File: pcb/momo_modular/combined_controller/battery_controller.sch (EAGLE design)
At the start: 38 parts, among them Q2 P-MOSFET, U1 XRP7659, U3 MCP1702, U4 PIC24F16KA101-X_PSSOP, U5 FLASH8MSOP8, U6 MCP73811

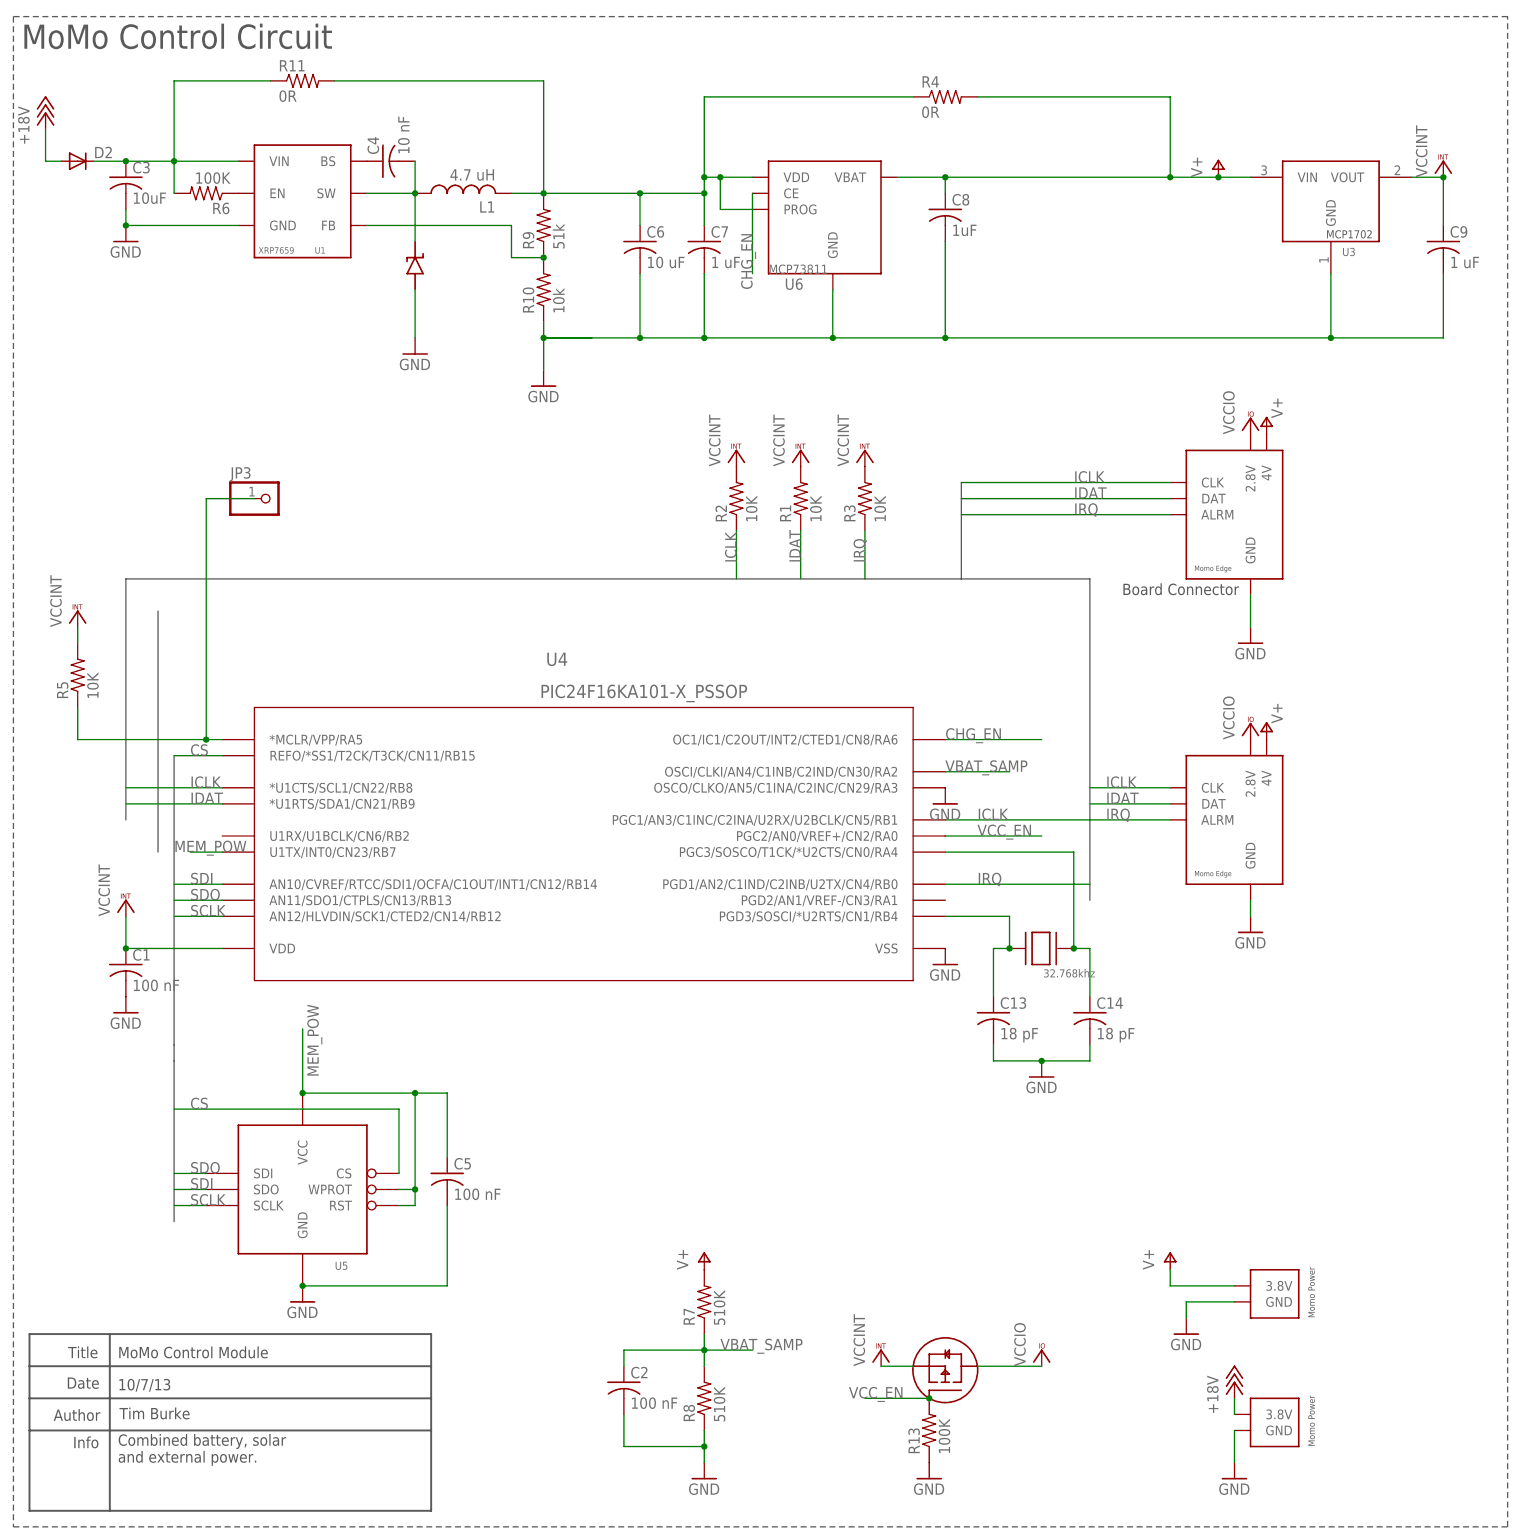
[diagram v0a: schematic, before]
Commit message: Finish initial layout of revised controller board with enhanced pic
- now has battery backup of RTC
- new pic24 chip with 64K rom and 8K RAM
- lower power consumption
- removed current meter to battery for charging current (just measure
  the voltage over time)
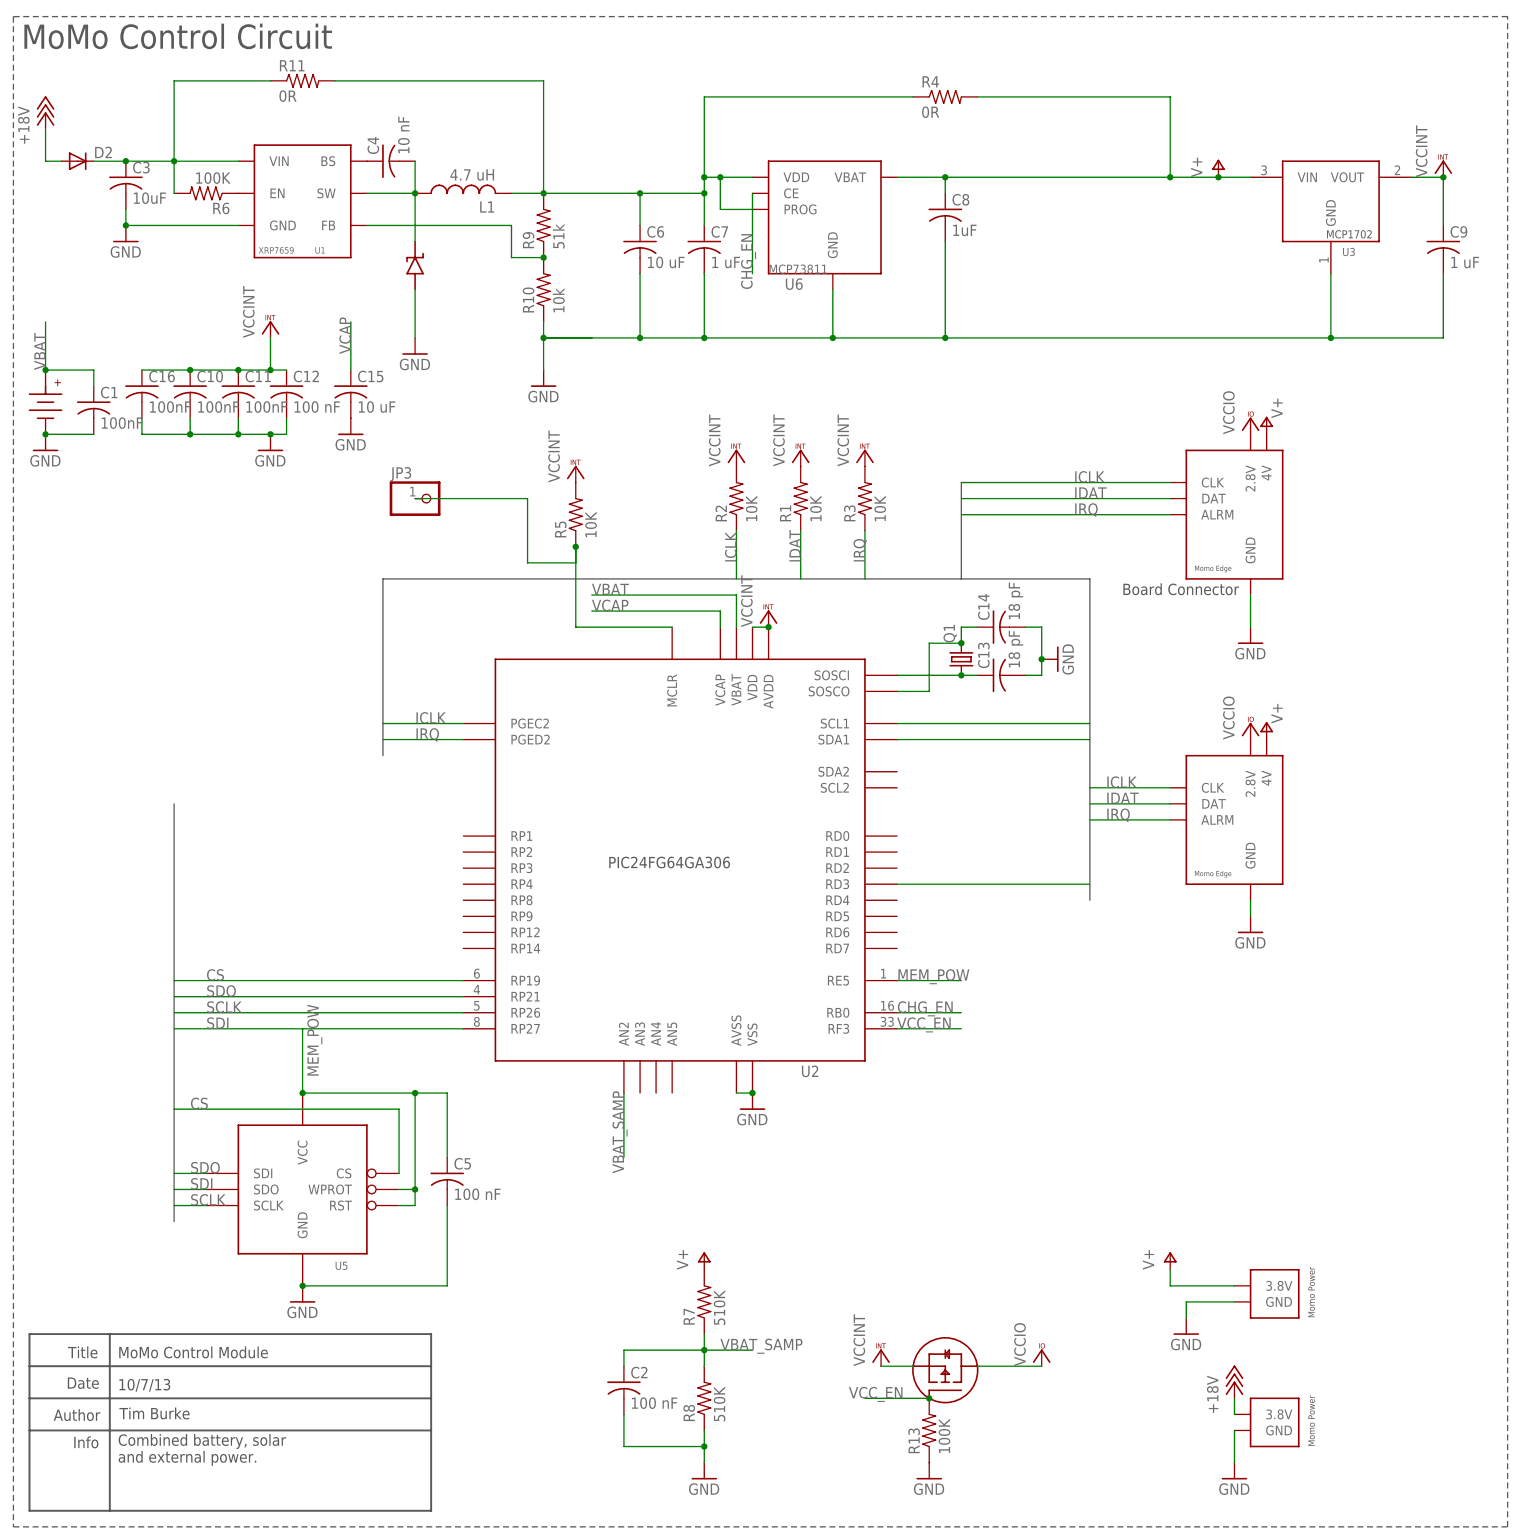
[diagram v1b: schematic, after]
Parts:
- removed U4: PIC24F16KA101-X_PSSOP, components:PIC24F16KA101-X_PSSOP
- removed XT1: 32.768khz, components:SMD-XTAL
- added BATT1: CR1025-HOLDER, components:CR1025-HOLDER
- added C10, C11, C16: 100nF, rcl:C-USC0402
- added C12: 100 nF, rcl:C-USC0402
- added C15: 10 uF, rcl:C-USC0805
- added Q1: (no value), crystal:CRYSTALTC26H
- added U2: PIC24FJ64GA306, components:PIC24FJ64GA306
- C1: value 100 nF -> 100nF; DIGIKEY-PN 445-1265-1-ND -> (none)
- R5: DIGIKEY-PN P10.0KHCT-ND -> (none)
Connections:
- removed net N$15: JP3.1, R5.1, U4.*MCLR/VPP/RA5
- removed net N$24: C14.1, U4.PGC3/SOSCO/T1CK/*U2CTS/CN0/RA4, XT1.XTAL2
- removed net N$25: C13.1, U4.PGD3/SOSCI/*U2RTS/CN1/RB4, XT1.XTAL1
- new net N$4: JP3.1, R5.1, U2.MCLR
- new net N$6: C14.1, Q1.2, U2.SOSCO
- new net N$7: C13.1, Q1.1, U2.SOSCI
- new net VBAT: BATT1.+, C1.1, U2.VBAT
- new net VCAP: C15.1, U2.VCAP
- net CHG_EN: now also U2.RB0; no longer U4.OC1/IC1/C2OUT/INT2/CTED1/CN8/RA6
- net CS: now also U2.RP19; no longer U4.REFO/*SS1/T2CK/T3CK/CN11/RB15
- net GND: now also BATT1.-, C10.2, C11.2, C12.2, C15.2, C16.2, U2.AVSS, U2.VSS; no longer U4.OSCO/CLKO/AN5/C1INA/C2INC/CN29/RA3, U4.VSS
- net ICLK: now also U2.PGEC2, U2.SCL1; no longer U4.*U1CTS/SCL1/CN22/RB8, U4.PGC1/AN3/C1INC/C2INA/U2RX/U2BCLK/CN5/RB1
- net IDAT: now also U2.SDA1; no longer U4.*U1RTS/SDA1/CN21/RB9
- net IRQ: now also U2.PGED2, U2.RD3; no longer U4.PGD1/AN2/C1IND/C2INB/U2TX/CN4/RB0
- net MEM_POW: now also U2.RE5; no longer U4.U1TX/INT0/CN23/RB7
- net SCLK: now also U2.RP26; no longer U4.AN12/HLVDIN/SCK1/CTED2/CN14/RB12
- net SDI: now also U2.RP27; no longer U4.AN10/CVREF/RTCC/SDI1/OCFA/C1OUT/INT1/CN12/RB14
- net SDO: now also U2.RP21; no longer U4.AN11/SDO1/CTPLS/CN13/RB13
- net VBAT_SAMP: now also U2.AN2; no longer U4.OSCI/CLKI/AN4/C1INB/C2IND/CN30/RA2
- net VCCINT: now also C10.1, C11.1, C12.1, C16.1, U2.AVDD, U2.VDD; no longer C1.1, U4.VDD
- net VCC_EN: now also U2.RF3; no longer U4.PGC2/AN0/VREF+/CN2/RA0
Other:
- moved on the sheet: C1, C13, C14, JP3, R5

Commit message: Finish laying out combined_controller board
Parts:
- C1, C10, C11, C12, C16: DIGIKEY-PN (none) -> 445-1265-1-ND
- D2: DESCRIPTION (none) -> Schottky Diode
- Q1: DIGIKEY-PN (none) -> 535-9034-ND
- R5: DIGIKEY-PN (none) -> P10.0KHCT-ND
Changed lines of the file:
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@@
 <?xml version="1.0" encoding="utf-8"?>
 <!DOCTYPE eagle SYSTEM "eagle.dtd">
-<eagle version="6.5.0">
+<eagle version="6.4">
 <drawing>
 <settings>
@@
 <part name="JP3" library="pinhead" deviceset="PINHD-1X1" device=""/>
 <part name="D2" library="diode" deviceset="DIODE-" device="DO214AC">
+<attribute name="DESCRIPTION" value="Schottky Diode "/>
 <attribute name="DIGIKEY-PN" value="SL13HE3/61TGICT-ND"/>
 </part>
@@
 <attribute name="DIGIKEY-PN-SOLAR" value="MCP73811T-420I/OTCT-ND"/>
 </part>
-<part name="Q1" library="crystal" deviceset="CRYSTAL" device="TC26H"/>
-<part name="R5" library="rcl" deviceset="R-US_" device="R0603" value="10K"/>
+<part name="Q1" library="crystal" deviceset="CRYSTAL" device="TC26H">
+<attribute name="DIGIKEY-PN" value="535-9034-ND"/>
+</part>
+<part name="R5" library="rcl" deviceset="R-US_" device="R0603" value="10K">
+<attribute name="DIGIKEY-PN" value="P10.0KHCT-ND"/>
+</part>
 <part name="VCC5" library="supply1" deviceset="VCCINT" device=""/>
 <part name="VCC6" library="supply1" deviceset="VCCINT" device=""/>
@@
 <part name="GND3" library="supply1" deviceset="GND" device=""/>
 <part name="U2" library="components" deviceset="PIC24FJ64GA306" device=""/>
-<part name="C1" library="rcl" deviceset="C-US" device="C0402" value="100nF"/>
-<part name="C10" library="rcl" deviceset="C-US" device="C0402" value="100nF"/>
-<part name="C11" library="rcl" deviceset="C-US" device="C0402" value="100nF"/>
-<part name="C12" library="rcl" deviceset="C-US" device="C0402" value="100 nF"/>
+<part name="C1" library="rcl" deviceset="C-US" device="C0402" value="100nF">
+<attribute name="DIGIKEY-PN" value="445-1265-1-ND"/>
+</part>
+<part name="C10" library="rcl" deviceset="C-US" device="C0402" value="100nF">
+<attribute name="DIGIKEY-PN" value="445-1265-1-ND"/>
+</part>
+<part name="C11" library="rcl" deviceset="C-US" device="C0402" value="100nF">
+<attribute name="DIGIKEY-PN" value="445-1265-1-ND"/>
+</part>
+<part name="C12" library="rcl" deviceset="C-US" device="C0402" value="100 nF">
+<attribute name="DIGIKEY-PN" value="445-1265-1-ND"/>
+</part>
 <part name="VCC7" library="supply1" deviceset="VCCINT" device=""/>
 <part name="GND5" library="supply1" deviceset="GND" device=""/>
@@
 </part>
 <part name="GND6" library="supply1" deviceset="GND" device=""/>
-<part name="C16" library="rcl" deviceset="C-US" device="C0402" value="100nF"/>
+<part name="C16" library="rcl" deviceset="C-US" device="C0402" value="100nF">
+<attribute name="DIGIKEY-PN" value="445-1265-1-ND"/>
+</part>
 </parts>
 <sheets>
@@
 <instance part="D2" gate="G$1" x="-215.9" y="104.14">
 <attribute name="DIGIKEY-PN" x="-215.9" y="104.14" size="1.778" layer="96" display="off"/>
+<attribute name="DESCRIPTION" x="-215.9" y="104.14" size="1.778" layer="96" display="off"/>
 </instance>
 <instance part="U6" gate="G$1" x="-106.68" y="93.98" smashed="yes">
@@
 <attribute name="DIGIKEY-PN-SOLAR" x="-106.68" y="93.98" size="1.778" layer="96" display="off"/>
 </instance>
-<instance part="Q1" gate="G$1" x="-76.2" y="25.4" rot="R90"/>
-<instance part="R5" gate="G$1" x="-137.16" y="48.26" rot="R90"/>
+<instance part="Q1" gate="G$1" x="-76.2" y="25.4" rot="R90">
+<attribute name="DIGIKEY-PN" x="-76.2" y="25.4" size="1.778" layer="96" rot="R90" display="off"/>
+</instance>
+<instance part="R5" gate="G$1" x="-137.16" y="48.26" rot="R90">
+<attribute name="DIGIKEY-PN" x="-137.16" y="48.26" size="1.778" layer="96" rot="R90" display="off"/>
+</instance>
 <instance part="VCC5" gate="G$1" x="-137.16" y="55.88"/>
 <instance part="VCC6" gate="G$1" x="-106.68" y="33.02"/>
@@
 <instance part="GND3" gate="1" x="-220.98" y="58.42"/>
 <instance part="U2" gate="G$1" x="-104.14" y="-7.62"/>
-<instance part="C1" gate="G$1" x="-213.36" y="66.04"/>
-<instance part="C10" gate="G$1" x="-198.12" y="68.58"/>
-<instance part="C11" gate="G$1" x="-190.5" y="68.58"/>
-<instance part="C12" gate="G$1" x="-182.88" y="68.58"/>
+<instance part="C1" gate="G$1" x="-213.36" y="66.04">
+<attribute name="DIGIKEY-PN" x="-213.36" y="66.04" size="1.778" layer="96" display="off"/>
+</instance>
+<instance part="C10" gate="G$1" x="-198.12" y="68.58">
+<attribute name="DIGIKEY-PN" x="-198.12" y="68.58" size="1.778" layer="96" display="off"/>
+</instance>
+<instance part="C11" gate="G$1" x="-190.5" y="68.58">
+<attribute name="DIGIKEY-PN" x="-190.5" y="68.58" size="1.778" layer="96" display="off"/>
+</instance>
+<instance part="C12" gate="G$1" x="-182.88" y="68.58">
+<attribute name="DIGIKEY-PN" x="-182.88" y="68.58" size="1.778" layer="96" display="off"/>
+</instance>
 <instance part="VCC7" gate="G$1" x="-185.42" y="78.74"/>
 <instance part="GND5" gate="1" x="-185.42" y="58.42"/>
@@
 </instance>
 <instance part="GND6" gate="1" x="-172.72" y="60.96"/>
-<instance part="C16" gate="G$1" x="-205.74" y="68.58"/>
+<instance part="C16" gate="G$1" x="-205.74" y="68.58">
+<attribute name="DIGIKEY-PN" x="-205.74" y="68.58" size="1.778" layer="96" display="off"/>
+</instance>
 </instances>
 <busses>
